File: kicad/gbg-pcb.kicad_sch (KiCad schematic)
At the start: 49 parts, among them J1 12 2.54mm pitch header pins, J2 Conn_01x02, J3 joystick, J4 speed knob, J5 TB005-762-02BE, J6 screw terminal, J7 1017491, J8 1017491, P1 rpi pico 1, Q1 PSMN1R2-25YLDX, Q2 PSMN1R2-25YLDX, SW1 screw terminal, U1 DRV8245HQPWPRQ1, U2 DRV8245HQPWPRQ1, U3 TPS54202HDDCR

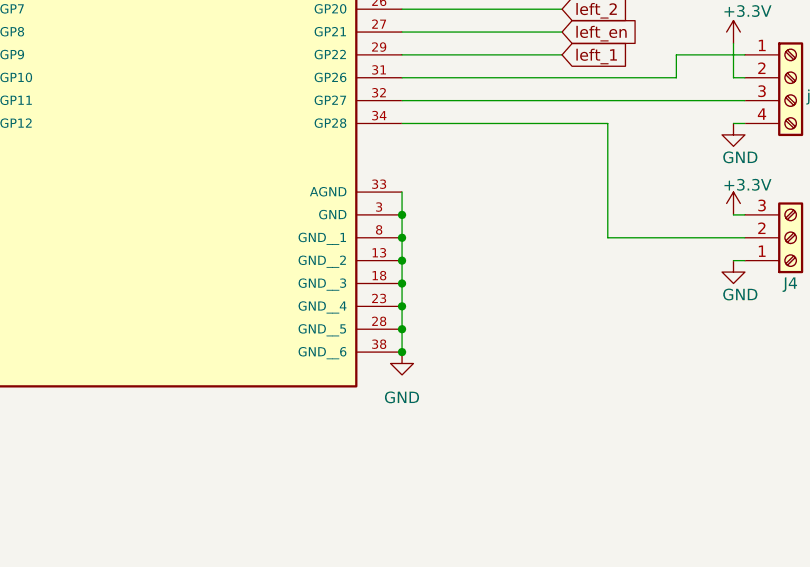
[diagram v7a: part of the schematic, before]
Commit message: draw traces
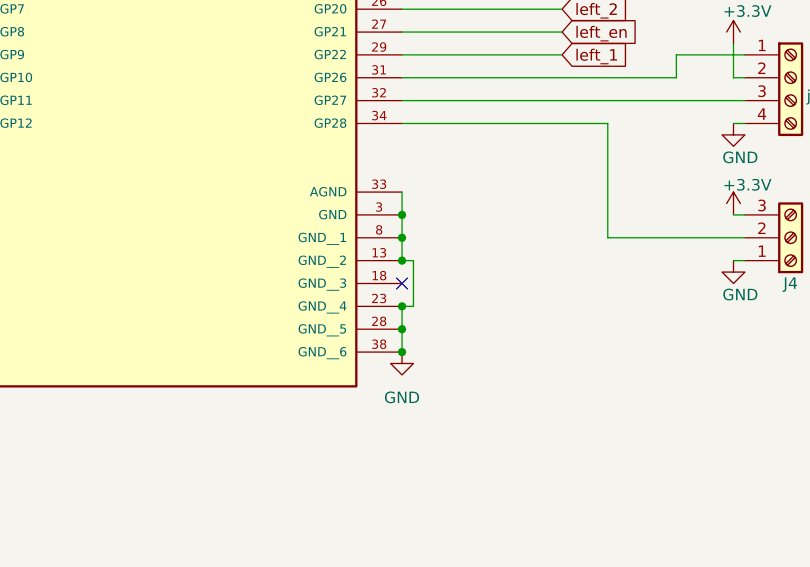
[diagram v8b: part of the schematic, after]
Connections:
- net GND: no longer P1.18 (GND__3)
- no-connect marks 10 -> 11
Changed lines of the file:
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@@
+	)
+	(junction
+		(at 99.06 101.6)
+		(diameter 0)
+		(color 0 0 0 0)
 	)
 	(junction
@@
 	)
 	(junction
-		(at 99.06 101.6)
-		(diameter 0)
-		(color 0 0 0 0)
-	)
-	(junction
 		(at 280.67 140.97)
 		(diameter 0)
@@
 	(junction
 		(at 99.06 109.22)
-		(diameter 0)
-		(color 0 0 0 0)
-	)
-	(junction
-		(at 99.06 104.14)
 		(diameter 0)
 		(color 0 0 0 0)
@@
 	)
 	(no_connect
+		(at 99.06 104.14)
+	)
+	(no_connect
 		(at 99.06 43.18)
 	)
@@
 	(wire
 		(pts
+			(xy 100.33 106.68) (xy 99.06 106.68)
+		)
+		(stroke
+			(width 0)
+			(type default)
+		)
+	)
+	(wire
+		(pts
 			(xy 26.67 68.58) (xy 48.26 68.58)
 		)
@@
 	(wire
 		(pts
-			(xy 99.06 104.14) (xy 99.06 106.68)
+			(xy 100.33 101.6) (xy 99.06 101.6)
 		)
 		(stroke
@@
 	(wire
 		(pts
-			(xy 99.06 101.6) (xy 99.06 104.14)
-		)
-		(stroke
+			(xy 100.33 101.6) (xy 100.33 106.68)
+		)
+		(stroke
